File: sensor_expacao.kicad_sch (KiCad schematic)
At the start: 47 parts, among them J10 Micro_SD_Card, J11 Conn_01x10, J12 ntc, J7 Micro_SD_Card, J8 Conn_01x11_Socket, J9 Conn_01x15_Pin, Q5 NMOS, Q6 NMOS, Q7 NMOS, U11 SRV05-4, U12 74HC4051

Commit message: 10082026/B
nova revisão
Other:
- company: (none) -> ---
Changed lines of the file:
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@@
 	(generator_version "10.0")
 	(paper "User" 431.8 279.4)
+	(title_block
+		(date "2026-08-10")
+		(rev "C")
+		(company "---")
+		(comment 1 "powered by STM32F407VET6")
+		(comment 2 "BY todio")
+		(comment 3 "na pagina \"hapia\" leia os aviosos e pergunta ")
+	)
 	(text "not\n"
 		(exclude_from_sim no)

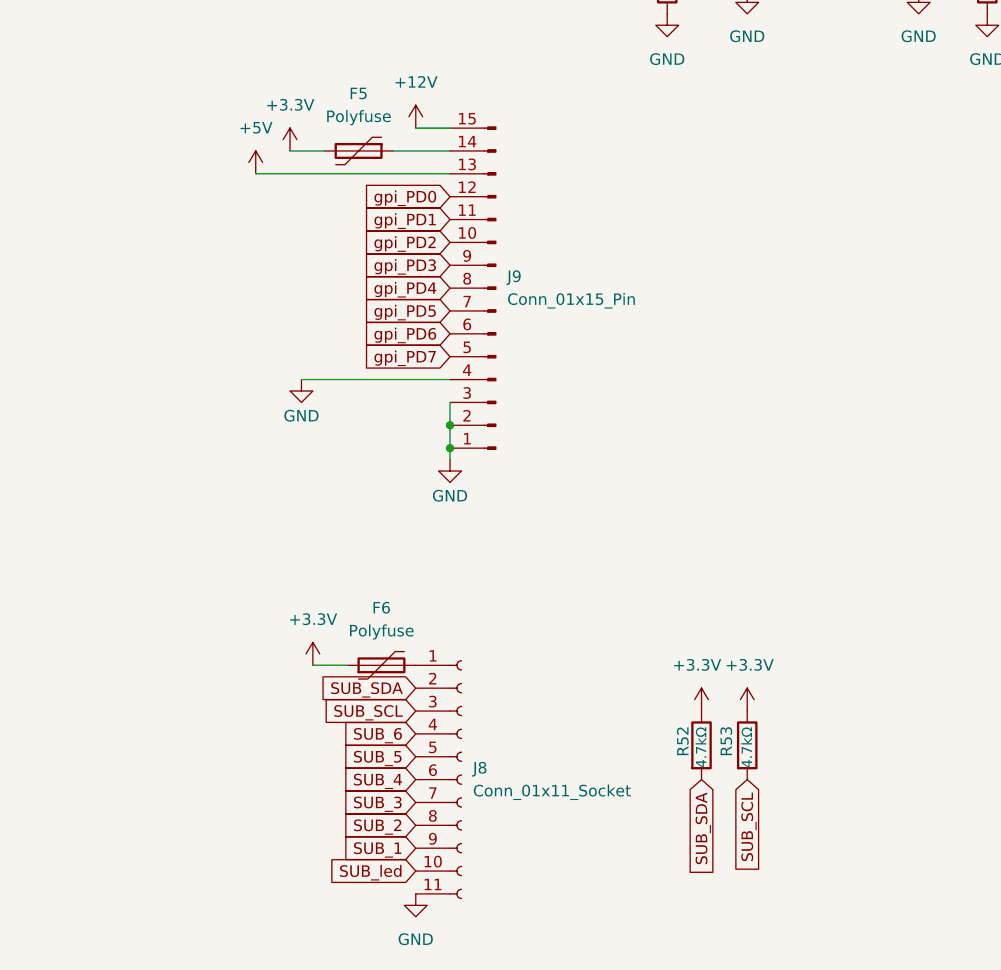
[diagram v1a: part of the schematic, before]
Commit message: 17082026/E
modulo FRAM e Melhoria no esquemático
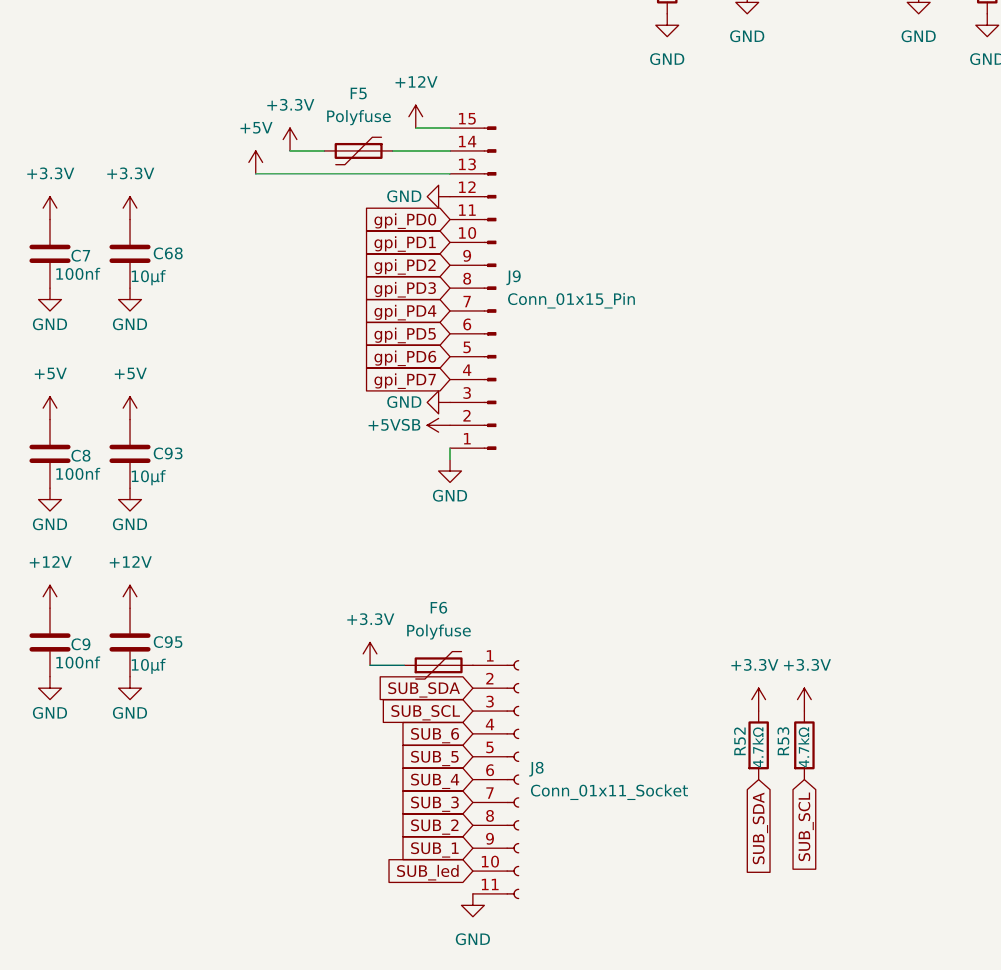
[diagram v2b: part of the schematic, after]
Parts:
- added C68, C93, C95: 10µf, symbol Device:C
- added C7, C8, C9: 100nf, Capacitor_SMD:C_0603_1608Metric, symbol Device:C
- J9: footprint Connector_PinSocket_2.54mm:PinSocket_1x15_P2.54mm_Vertical -> Connector_PinHeader_2.54mm:PinHeader_1x15_P2.54mm_Vertical
- U12: Descrição (none) -> e uma mux/demux bidiresonal para os ntc
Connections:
- net +12V: now also C9.1, C95.1
- net +3.3V: now also C68.1, C7.1
- net +5V: now also C8.1, C93.1
- net GND: now also J9.12 (Pin_12), C68.2, C7.2, C8.2, C9.2, C93.2, C95.2; no longer J9.2 (Pin_2), J9.4 (Pin_4)
- net gpi_PD0: now also J9.11 (Pin_11); no longer J9.12 (Pin_12)
- net gpi_PD1: now also J9.10 (Pin_10); no longer J9.11 (Pin_11)
- net gpi_PD2: now also J9.9 (Pin_9); no longer J9.10 (Pin_10)
- net gpi_PD3: now also J9.8 (Pin_8); no longer J9.9 (Pin_9)
- net gpi_PD4: now also J9.7 (Pin_7); no longer J9.8 (Pin_8)
- net gpi_PD5: now also J9.6 (Pin_6); no longer J9.7 (Pin_7)
- net gpi_PD6: now also J9.5 (Pin_5); no longer J9.6 (Pin_6)
- net gpi_PD7: now also J9.4 (Pin_4); no longer J9.5 (Pin_5)
- new net +5VSB: J9.2 (Pin_2)
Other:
- moved on the sheet: F6, J8, R52, R53

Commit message: 21082026/G
falta muita coisa
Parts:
- renumbered C7 to C70, C8 to C71, C9 to C72, C68 to C73, C93 to C74, C95 to C75, C72 to C76, C73 to C77, C74 to C78, C75 to C79, C76 to C80, C77 to C81, C78 to C82, C79 to C83, C80 to C84, C81 to C85, C82 to C86, F6 to F10, F5 to F9, J8 to J10, J10 to J11, J11 to J12, J12 to J13, J7 to J8, JP2 to JP3, JP3 to JP4, JP4 to JP5, Q5 to Q6, Q6 to Q7, Q7 to Q8, R50 to R85, R51 to R86, R52 to R87, R53 to R88, R54 to R89, R55 to R90, R56 to R91, R57 to R92, R58 to R93, R59 to R94, R60 to R95, R61 to R96, R62 to R97, R63 to R98, R64 to R99, U12 to U10, U11 to U9

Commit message: 29082026/I
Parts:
- removed C84, C86: 10nf, symbol Device:C
- removed J11: Micro_SD_Card, symbol Connector:Micro_SD_Card
- removed J13: ntc, symbol Connector_Generic:Conn_01x06
- removed JP3: ntc1, symbol Jumper:SolderJumper_2_Bridged
- removed JP4, JP5: ntc2, symbol Jumper:SolderJumper_2_Bridged
- removed Q6, Q7, Q8: NMOS, symbol Simulation_SPICE:NMOS
- removed R85, R90: 3.3kΩ, symbol Device:R
- removed R86, R89, R91, R95, R97, R99: 10kΩ, symbol Device:R
- removed TH1: 10k, symbol Device:Thermistor_NTC
- added C95, C96, C97, C98: 10nf, symbol Device:C
- added R114, R115, R116, R117: 10kΩ, symbol Device:R
- added TH10, TH6, TH7, TH8, TH9: 10kΩ, Resistor_SMD:R_0603_1608Metric, symbol Device:Thermistor_NTC
- C70, C71, C72, C76, C78: jlc_pcb: C346191 -> C307348; mouser: (none) -> 187-CL10B104KB8WPNC; mpn CL10B104KB8NFNC -> CL10B104KB8WPNC
- C82: value 10nf -> 10µf
- J8: footprint (none) -> Connector_Card:microSD_HC_Molex_47219-2001; jlc_pcb: (none) -> C164170; mouser: (none) -> 538-47219-2001; mpn (none) -> 472192001
- TH2, TH3, TH4: value 10k -> 10kΩ; footprint (none) -> Resistor_SMD:R_0603_1608Metric; jlc_pcb: (none) -> C13564; mouser: (none) -> 81-NCP18XH103F03RB; mpn (none) -> NCP18XH103F03RB
- TH5: value 10k -> 10kΩ
- U10: footprint Package_DIP:DIP-16_W7.62mm -> Package_SO:SOIC-16_3.9x9.9mm_P1.27mm; mouser: (none) -> 771-74HC4051D-T
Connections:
- net +3.3V: now also C82.1, TH10.1, TH6.1, TH7.1, TH8.1, TH9.1
- net GND: now also C95.2, C96.2, C97.2, C98.2, R114.2, R115.2, R116.2, R117.2; no longer U10.6 (~{E})
- net NTC_EX: now also TH3.2
- net NTC_ref: no longer U10.1 (A4)
- net NTC_driver_2: now reaches U10.5 (A5)
- net NTC_driver_2: now also C96.1, R115.1, TH8.2
- net NTC_driver_3: now reaches U10.2 (A6)
- net NTC_driver_3: now also C97.1, R116.1, TH9.2
- net NTC_driver_4: now reaches U10.4 (A7)
- net NTC_driver_4: now also C98.1, R117.1, TH10.2
- net NTC_driver renamed NTC_driver_1
- net NTC_driver_1: now also U10.1 (A4), TH7.2; no longer TH3.2, U10.15 (A2)
- net NTC_mosfet renamed NTC_mosfet_1
- net NTC_mosfet_1: now also U10.15 (A2); no longer U10.12 (A3)
- new net MUX_EN: U10.6 (~{E})
- new net NTC_mosfet_2: C95.1, R114.1, TH6.2, U10.12 (A3)
- no-connect marks 4 -> 2
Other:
- note removed: "not"
- moved on the sheet: C79, C80, C81, C83, C85, R92, R93, R94, R96, R98, TH2

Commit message: o .bom não foi terminado
O desafio e todo custar menos de 150 dólares(eua) e menos de 1000r(reais)
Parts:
- C73, C74, C75, C82: footprint (none) -> Capacitor_SMD:C_1206_3216Metric_Pad1.33x1.80mm_HandSolder; jlc_pcb: (none) -> C13585; mouser: (none) -> 187-CL31B106KLK6PNE; mpn (none) -> CL31A106KBHNNNE
- C77: value 10uf -> 10µf; footprint (none) -> Capacitor_SMD:C_1206_3216Metric_Pad1.33x1.80mm_HandSolder; jlc_pcb: (none) -> C13585; mouser: (none) -> 187-CL31B106KLK6PNE; mpn (none) -> CL31A106KBHNNNE
- C79, C80, C81, C83, C85, C95, C96, C97, C98: footprint (none) -> Capacitor_SMD:C_0402_1005Metric_Pad0.74x0.62mm_HandSolder; jlc_pcb: (none) -> C15195; mouser: (none) -> 187-CL05B103KB5NNNC; mpn (none) -> CL05B103KB5NNNC
- TH5: footprint (none) -> Resistor_SMD:R_0603_1608Metric
- U9: value SRV05-4 -> SRV05-4HTG-D; jlc_pcb: ssss -> C1975211; mouser: (none) -> 576-SRV05-4HTG-D; mpn ssss -> SRV05-4HTG-D

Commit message: 05092026/00001
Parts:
- R114, R115, R116, R117, R92, R93, R94, R96, R98: footprint (none) -> Resistor_SMD:R_0603_1608Metric Resistor_SMD:R_0603_1608Metric; jlc_pcb: (none) -> C13564; mouser: (none) -> 81-NCP18XH103F03RB; mpn (none) -> NCP18XH103F03RB
- R87, R88: footprint (none) -> Resistor_SMD:R_0603_1608Metric_Pad0.98x0.95mm_HandSolder; jlc_pcb: (none) -> C99782; mouser: (none) -> 603-RC0603FR-074K7L; mpn (none) -> RC0603FR-074K7L
- TH10, TH2, TH3, TH4, TH6, TH7, TH8, TH9: footprint Resistor_SMD:R_0603_1608Metric -> Resistor_SMD:R_0603_1608Metric Resistor_SMD:R_0603_1608Metric
- TH5: footprint Resistor_SMD:R_0603_1608Metric -> Resistor_SMD:R_0603_1608Metric Resistor_SMD:R_0603_1608Metric; jlc_pcb: (none) -> C13564; mouser: (none) -> 81-NCP18XH103F03RB; mpn (none) -> NCP18XH103F03RB

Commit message: 27092026/0002
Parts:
- R114, R115, R116, R117, R92, R93, R94, R96, R98, TH10, TH2, TH3, TH4, TH5, TH6, TH7, TH8, TH9: footprint Resistor_SMD:R_0603_1608Metric Resistor_SMD:R_0603_1608Metric -> Resistor_SMD:R_0603_1608Metric Resistor_SMD_R_0603_1608Metric
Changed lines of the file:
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@@
 			)
 		)
-		(property "Footprint" "Resistor_SMD:R_0603_1608Metric Resistor_SMD:R_0603_1608Metric"
+		(property "Footprint" "Resistor_SMD:R_0603_1608Metric Resistor_SMD_R_0603_1608Metric"
 			(at 287.02 59.69 0)
 			(hide yes)
@@
 			)
 		)
-		(property "Footprint" "Resistor_SMD:R_0603_1608Metric Resistor_SMD:R_0603_1608Metric"
+		(property "Footprint" "Resistor_SMD:R_0603_1608Metric Resistor_SMD_R_0603_1608Metric"
 			(at 347.98 59.69 0)
 			(hide yes)
@@
 			)
 		)
-		(property "Footprint" "Resistor_SMD:R_0603_1608Metric Resistor_SMD:R_0603_1608Metric"
+		(property "Footprint" "Resistor_SMD:R_0603_1608Metric Resistor_SMD_R_0603_1608Metric"
 			(at 368.3 59.69 0)
 			(hide yes)
@@
 			)
 		)
-		(property "Footprint" "Resistor_SMD:R_0603_1608Metric Resistor_SMD:R_0603_1608Metric"
+		(property "Footprint" "Resistor_SMD:R_0603_1608Metric Resistor_SMD_R_0603_1608Metric"
 			(at 262.255 22.86 0)
 			(hide yes)
@@
 			)
 		)
-		(property "Footprint" "Resistor_SMD:R_0603_1608Metric Resistor_SMD:R_0603_1608Metric"
+		(property "Footprint" "Resistor_SMD:R_0603_1608Metric Resistor_SMD_R_0603_1608Metric"
 			(at 388.62 59.69 0)
 			(hide yes)
@@
 			)
 		)
-		(property "Footprint" "Resistor_SMD:R_0603_1608Metric Resistor_SMD:R_0603_1608Metric"
+		(property "Footprint" "Resistor_SMD:R_0603_1608Metric Resistor_SMD_R_0603_1608Metric"
 			(at 243.332 68.58 90)
 			(hide yes)
@@
 			)
 		)
-		(property "Footprint" "Resistor_SMD:R_0603_1608Metric Resistor_SMD:R_0603_1608Metric"
+		(property "Footprint" "Resistor_SMD:R_0603_1608Metric Resistor_SMD_R_0603_1608Metric"
 			(at 245.11 59.69 0)
 			(hide yes)
@@
 			)
 		)
-		(property "Footprint" "Resistor_SMD:R_0603_1608Metric Resistor_SMD:R_0603_1608Metric"
+		(property "Footprint" "Resistor_SMD:R_0603_1608Metric Resistor_SMD_R_0603_1608Metric"
 			(at 327.66 59.69 0)
 			(hide yes)
@@
 			)
 		)
-		(property "Footprint" "Resistor_SMD:R_0603_1608Metric Resistor_SMD:R_0603_1608Metric"
+		(property "Footprint" "Resistor_SMD:R_0603_1608Metric Resistor_SMD_R_0603_1608Metric"
 			(at 305.562 68.58 90)
 			(hide yes)
@@
 			)
 		)
-		(property "Footprint" "Resistor_SMD:R_0603_1608Metric Resistor_SMD:R_0603_1608Metric"
+		(property "Footprint" "Resistor_SMD:R_0603_1608Metric Resistor_SMD_R_0603_1608Metric"
 			(at 264.287 68.58 90)
 			(hide yes)
@@
 			)
 		)
-		(property "Footprint" "Resistor_SMD:R_0603_1608Metric Resistor_SMD:R_0603_1608Metric"
+		(property "Footprint" "Resistor_SMD:R_0603_1608Metric Resistor_SMD_R_0603_1608Metric"
 			(at 325.882 68.58 90)
 			(hide yes)
@@
 			)
 		)
-		(property "Footprint" "Resistor_SMD:R_0603_1608Metric Resistor_SMD:R_0603_1608Metric"
+		(property "Footprint" "Resistor_SMD:R_0603_1608Metric Resistor_SMD_R_0603_1608Metric"
 			(at 260.477 31.75 90)
 			(hide yes)
@@
 			)
 		)
-		(property "Footprint" "Resistor_SMD:R_0603_1608Metric Resistor_SMD:R_0603_1608Metric"
+		(property "Footprint" "Resistor_SMD:R_0603_1608Metric Resistor_SMD_R_0603_1608Metric"
 			(at 346.202 68.58 90)
 			(hide yes)
@@
 			)
 		)
-		(property "Footprint" "Resistor_SMD:R_0603_1608Metric Resistor_SMD:R_0603_1608Metric"
+		(property "Footprint" "Resistor_SMD:R_0603_1608Metric Resistor_SMD_R_0603_1608Metric"
 			(at 266.065 59.69 0)
 			(hide yes)
@@
 			)
 		)
-		(property "Footprint" "Resistor_SMD:R_0603_1608Metric Resistor_SMD:R_0603_1608Metric"
+		(property "Footprint" "Resistor_SMD:R_0603_1608Metric Resistor_SMD_R_0603_1608Metric"
 			(at 366.522 68.58 90)
 			(hide yes)
@@
 			)
 		)
-		(property "Footprint" "Resistor_SMD:R_0603_1608Metric Resistor_SMD:R_0603_1608Metric"
+		(property "Footprint" "Resistor_SMD:R_0603_1608Metric Resistor_SMD_R_0603_1608Metric"
 			(at 386.842 68.58 90)
 			(hide yes)
@@
 			)
 		)
-		(property "Footprint" "Resistor_SMD:R_0603_1608Metric Resistor_SMD:R_0603_1608Metric"
+		(property "Footprint" "Resistor_SMD:R_0603_1608Metric Resistor_SMD_R_0603_1608Metric"
 			(at 307.34 59.69 0)
 			(hide yes)
@@
 			)
 		)
-		(property "Footprint" "Resistor_SMD:R_0603_1608Metric Resistor_SMD:R_0603_1608Metric"
+		(property "Footprint" "Resistor_SMD:R_0603_1608Metric Resistor_SMD_R_0603_1608Metric"
 			(at 285.242 68.58 90)
 			(hide yes)
